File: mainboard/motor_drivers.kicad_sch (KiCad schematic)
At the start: 32 parts, among them J10 CON_CONNAXIO_MOTOR_DRIVER, J11 CON_CONNAXIO_MOTOR_DRIVER, J12 CON_CONNAXIO_MOTOR_DRIVER, J13 CON_CONNAXIO_MOTOR_DRIVER, J14 CON_CONNAXIO_MOTOR_DRIVER, J5 CON_CONNAXIO_MOTOR_DRIVER, J6 CON_CONNAXIO_MOTOR_DRIVER, J7 CON_CONNAXIO_MOTOR_DRIVER, J8 CON_CONNAXIO_MOTOR_DRIVER, J9 CON_CONNAXIO_MOTOR_DRIVER

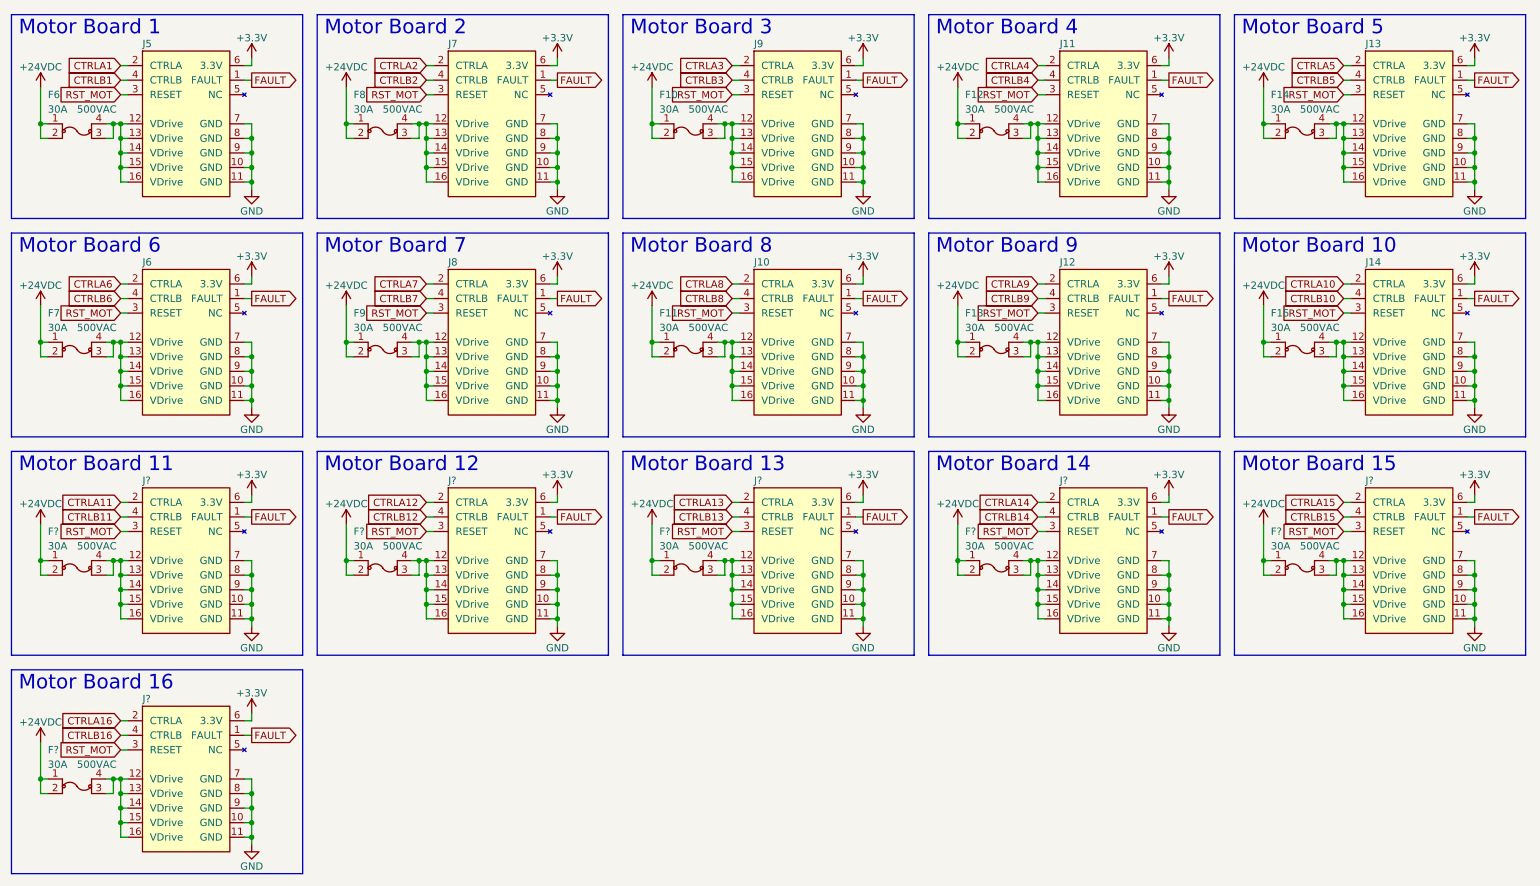
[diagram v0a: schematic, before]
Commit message: Move fuse to motor driver board Optimize board array schematic (hierarchical schematics)
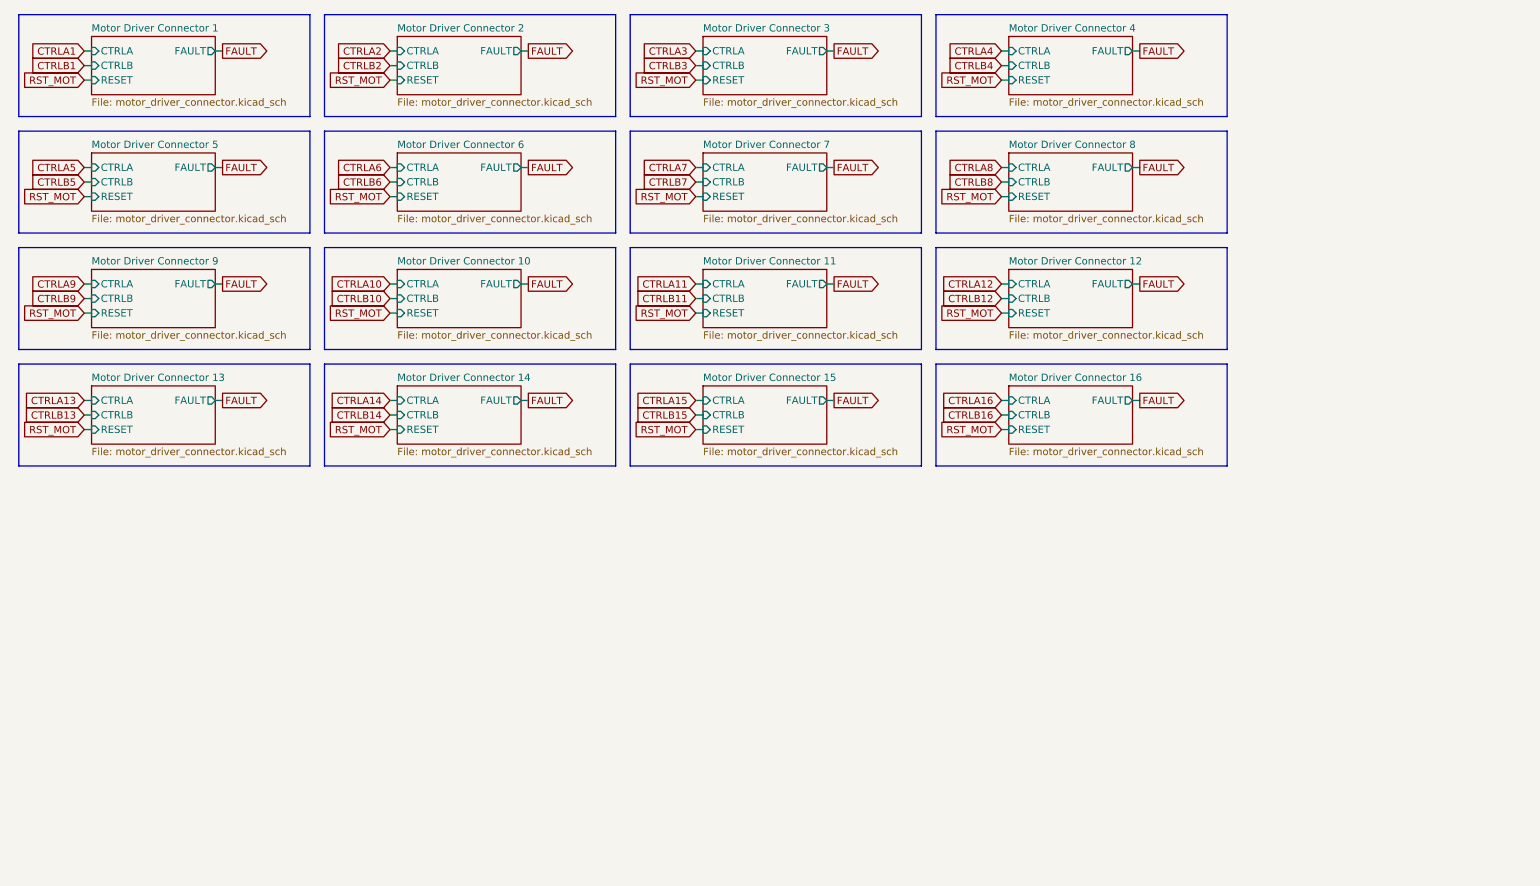
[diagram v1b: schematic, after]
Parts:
- removed F10, F11, F12, F13, F14, F15, F6, F7, F8, F9, F? (x6): FUS_BLADE_3522, connaxio-connectors:FUS_BLADE_3522, symbol connaxio-connectors:FUS_BLADE_3522
- removed J10, J11, J12, J13, J14, J5, J6, J7, J8, J9, J? (x6): CON_CONNAXIO_MOTOR_DRIVER, connaxio-connectors:CON_HDR_100MILS_F_TH_2X8, symbol connaxio-connectors:CON_CONNAXIO_MOTOR_DRIVER
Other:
- added sheet Motor Driver Connector 1 (motor_driver_connector.kicad_sch)
- added sheet Motor Driver Connector 10 (motor_driver_connector.kicad_sch)
- added sheet Motor Driver Connector 11 (motor_driver_connector.kicad_sch)
- added sheet Motor Driver Connector 12 (motor_driver_connector.kicad_sch)
- added sheet Motor Driver Connector 13 (motor_driver_connector.kicad_sch)
- added sheet Motor Driver Connector 14 (motor_driver_connector.kicad_sch)
- added sheet Motor Driver Connector 15 (motor_driver_connector.kicad_sch)
- added sheet Motor Driver Connector 16 (motor_driver_connector.kicad_sch)
- added sheet Motor Driver Connector 2 (motor_driver_connector.kicad_sch)
- added sheet Motor Driver Connector 3 (motor_driver_connector.kicad_sch)
- added sheet Motor Driver Connector 4 (motor_driver_connector.kicad_sch)
- added sheet Motor Driver Connector 5 (motor_driver_connector.kicad_sch)
- added sheet Motor Driver Connector 6 (motor_driver_connector.kicad_sch)
- added sheet Motor Driver Connector 7 (motor_driver_connector.kicad_sch)
- added sheet Motor Driver Connector 8 (motor_driver_connector.kicad_sch)
- added sheet Motor Driver Connector 9 (motor_driver_connector.kicad_sch)
- note removed: "Motor Board 1"
- note removed: "Motor Board 10"
- note removed: "Motor Board 11"
- note removed: "Motor Board 12"
- note removed: "Motor Board 13"
- note removed: "Motor Board 14"
- note removed: "Motor Board 15"
- note removed: "Motor Board 16"
- note removed: "Motor Board 2"
- note removed: "Motor Board 3"
- note removed: "Motor Board 4"
- note removed: "Motor Board 5"
- note removed: "Motor Board 6"
- note removed: "Motor Board 7"
- note removed: "Motor Board 8"
- note removed: "Motor Board 9"

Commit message: Inverted motor controls for open-drain operation and manual switch override compatibility
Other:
- sheet Motor Driver Connector 1 ports: added ~{CTRLA}, ~{CTRLB}, ~{FAULT}, ~{RESET}; removed CTRLA, CTRLB, FAULT, RESET
- sheet Motor Driver Connector 10 ports: added ~{CTRLA}, ~{CTRLB}, ~{FAULT}, ~{RESET}; removed CTRLA, CTRLB, FAULT, RESET
- sheet Motor Driver Connector 11 ports: added ~{CTRLA}, ~{CTRLB}, ~{FAULT}, ~{RESET}; removed CTRLA, CTRLB, FAULT, RESET
- sheet Motor Driver Connector 12 ports: added ~{CTRLA}, ~{CTRLB}, ~{FAULT}, ~{RESET}; removed CTRLA, CTRLB, FAULT, RESET
- sheet Motor Driver Connector 13 ports: added ~{CTRLA}, ~{CTRLB}, ~{FAULT}, ~{RESET}; removed CTRLA, CTRLB, FAULT, RESET
- sheet Motor Driver Connector 14 ports: added ~{CTRLA}, ~{CTRLB}, ~{FAULT}, ~{RESET}; removed CTRLA, CTRLB, FAULT, RESET
- sheet Motor Driver Connector 15 ports: added ~{CTRLA}, ~{CTRLB}, ~{FAULT}, ~{RESET}; removed CTRLA, CTRLB, FAULT, RESET
- sheet Motor Driver Connector 16 ports: added ~{CTRLA}, ~{CTRLB}, ~{FAULT}, ~{RESET}; removed CTRLA, CTRLB, FAULT, RESET
- sheet Motor Driver Connector 2 ports: added ~{CTRLA}, ~{CTRLB}, ~{FAULT}, ~{RESET}; removed CTRLA, CTRLB, FAULT, RESET
- sheet Motor Driver Connector 3 ports: added ~{CTRLA}, ~{CTRLB}, ~{FAULT}, ~{RESET}; removed CTRLA, CTRLB, FAULT, RESET
- sheet Motor Driver Connector 4 ports: added ~{CTRLA}, ~{CTRLB}, ~{FAULT}, ~{RESET}; removed CTRLA, CTRLB, FAULT, RESET
- sheet Motor Driver Connector 5 ports: added ~{CTRLA}, ~{CTRLB}, ~{FAULT}, ~{RESET}; removed CTRLA, CTRLB, FAULT, RESET
- sheet Motor Driver Connector 6 ports: added ~{CTRLA}, ~{CTRLB}, ~{FAULT}, ~{RESET}; removed CTRLA, CTRLB, FAULT, RESET
- sheet Motor Driver Connector 7 ports: added ~{CTRLA}, ~{CTRLB}, ~{FAULT}, ~{RESET}; removed CTRLA, CTRLB, FAULT, RESET
- sheet Motor Driver Connector 8 ports: added ~{CTRLA}, ~{CTRLB}, ~{FAULT}, ~{RESET}; removed CTRLA, CTRLB, FAULT, RESET
- sheet Motor Driver Connector 9 ports: added ~{CTRLA}, ~{CTRLB}, ~{FAULT}, ~{RESET}; removed CTRLA, CTRLB, FAULT, RESET

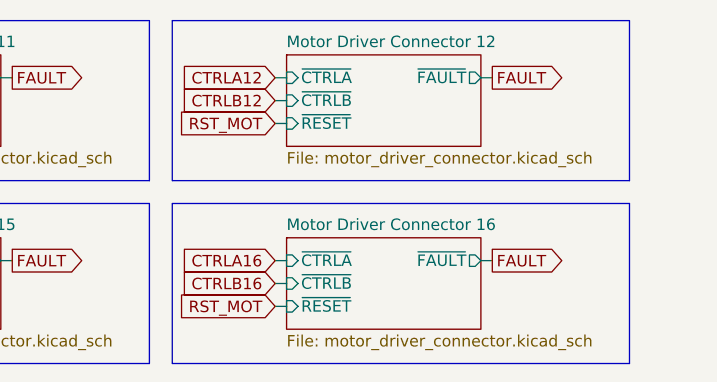
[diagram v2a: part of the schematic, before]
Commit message: Position drive rmodules, choose enclosure, shape PCB
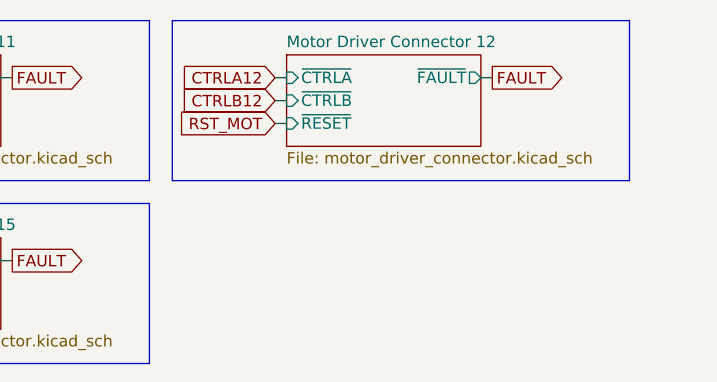
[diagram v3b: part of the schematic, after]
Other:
- removed sheet Motor Driver Connector 16
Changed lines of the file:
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@@
-    (stroke (width 0) (type default) (color 0 0 0 0))
-  )
-  (wire (pts (xy 186.69 87.63) (xy 187.96 87.63))
     (stroke (width 0) (type default) (color 0 0 0 0))
   )
@@
     (stroke (width 0) (type default) (color 0 0 0 0))
   )
-  (polyline (pts (xy 175.26 93.98) (xy 226.06 93.98))
-    (stroke (width 0) (type default) (color 0 0 0 0))
-  )
   (polyline (pts (xy 68.58 35.56) (xy 68.58 53.34))
     (stroke (width 0) (type default) (color 0 0 0 0))
@@
     (stroke (width 0) (type default) (color 0 0 0 0))
   )
-  (polyline (pts (xy 226.06 93.98) (xy 226.06 76.2))
-    (stroke (width 0) (type default) (color 0 0 0 0))
-  )
   (polyline (pts (xy 226.06 53.34) (xy 226.06 35.56))
     (stroke (width 0) (type default) (color 0 0 0 0))
@@
     (stroke (width 0) (type default) (color 0 0 0 0))
   )
-  (wire (pts (xy 209.55 82.55) (xy 210.82 82.55))
-    (stroke (width 0) (type default) (color 0 0 0 0))
-  )
-  (wire (pts (xy 186.69 82.55) (xy 187.96 82.55))
-    (stroke (width 0) (type default) (color 0 0 0 0))
-  )
   (wire (pts (xy 186.69 46.99) (xy 187.96 46.99))
     (stroke (width 0) (type default) (color 0 0 0 0))
@@
     (stroke (width 0) (type default) (color 0 0 0 0))
   )
-  (polyline (pts (xy 175.26 76.2) (xy 175.26 93.98))
-    (stroke (width 0) (type default) (color 0 0 0 0))
-  )
   (polyline (pts (xy 175.26 15.24) (xy 226.06 15.24))
     (stroke (width 0) (type default) (color 0 0 0 0))
   )
-  (polyline (pts (xy 175.26 76.2) (xy 226.06 76.2))
-    (stroke (width 0) (type default) (color 0 0 0 0))
-  )
   (wire (pts (xy 80.01 62.23) (xy 81.28 62.23))
     (stroke (width 0) (type default) (color 0 0 0 0))
@@
     (stroke (width 0) (type default) (color 0 0 0 0))
   )
-  (wire (pts (xy 186.69 85.09) (xy 187.96 85.09))
-    (stroke (width 0) (type default) (color 0 0 0 0))
-  )
   (wire (pts (xy 26.67 44.45) (xy 27.94 44.45))
     (stroke (width 0) (type default) (color 0 0 0 0))
@@
     )
   )
-  (global_label "CTRLA16" (shape input) (at 186.69 82.55 180) (fields_autoplaced)
-    (effects (font (size 1.27 1.27)) (justify right))
-    (property "Intersheet References" "${INTERSHEET_REFS}" (id 0) (at 176.3225 82.4706 0)
-      (effects (font (size 1.27 1.27)) (justify right) hide)
-    )
-  )
-  (global_label "RST_MOT" (shape input) (at 186.69 87.63 180) (fields_autoplaced)
-    (effects (font (size 1.27 1.27)) (justify right))
-    (property "Intersheet References" "${INTERSHEET_REFS}" (id 0) (at 176.2015 87.5506 0)
-      (effects (font (size 1.27 1.27)) (justify right) hide)
-    )
-  )
   (global_label "RST_MOT" (shape input) (at 133.35 46.99 180) (fields_autoplaced)
     (effects (font (size 1.27 1.27)) (justify right))
@@
     )
   )
-  (global_label "CTRLB16" (shape input) (at 186.69 85.09 180) (fields_autoplaced)
-    (effects (font (size 1.27 1.27)) (justify right))
-    (property "Intersheet References" "${INTERSHEET_REFS}" (id 0) (at 176.141 85.0106 0)
-      (effects (font (size 1.27 1.27)) (justify right) hide)
-    )
-  )
   (global_label "CTRLA12" (shape input) (at 186.69 62.23 180) (fields_autoplaced)
     (effects (font (size 1.27 1.27)) (justify right))
@@
     (property "Intersheet References" "${INTERSHEET_REFS}" (id 0) (at 70.6706 24.0506 0)
       (effects (font (size 1.27 1.27)) (justify right) hide)
-    )
-  )
-  (global_label "FAULT" (shape output) (at 210.82 82.55 0) (fields_autoplaced)
-    (effects (font (size 1.27 1.27)) (justify left))
-    (property "Intersheet References" "${INTERSHEET_REFS}" (id 0) (at 218.6475 82.4706 0)
-      (effects (font (size 1.27 1.27)) (justify left) hide)
     )
   )
@@
       (effects (font (size 1.27 1.27)) (justify left))
     )
-  )
-  (sheet (at 187.96 80.01) (size 21.59 10.16) (fields_autoplaced)
-    (stroke (width 0.1524) (type solid) (color 0 0 0 0))
-    (fill (color 0 0 0 0.0000))
-    (property "Sheet name" "Motor Driver Connector 16" (id 0) (at 187.96 79.2984 0)
-      (effects (font (size 1.27 1.27)) (justify left bottom))
-    )
-    (property "Sheet file" "motor_driver_connector.kicad_sch" (id 1) (at 187.96 90.7546 0)
-      (effects (font (size 1.27 1.27)) (justify left top))
-    )
-    (pin "~{FAULT}" output (at 209.55 82.55 0)
-      (effects (font (size 1.27 1.27)) (justify right))
-    )
-    (pin "~{RESET}" input (at 187.96 87.63 180)
-      (effects (font (size 1.27 1.27)) (justify left))
-    )
-    (pin "~{CTRLA}" input (at 187.96 82.55 180)
-      (effects (font (size 1.27 1.27)) (justify left))
-    )
-    (pin "~{CTRLB}" input (at 187.96 85.09 180)
-      (effects (font (size 1.27 1.27)) (justify left))
-    )
